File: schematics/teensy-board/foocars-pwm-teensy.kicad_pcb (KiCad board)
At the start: 2 copper layers, 26.4 x 36.6 mm, 4 parts, among them J1 TOPTOP-14-LEFT, J2 BOTTOMBOTTOM-14-LEFT, J3 PWM_Input, J4 PWM_Output

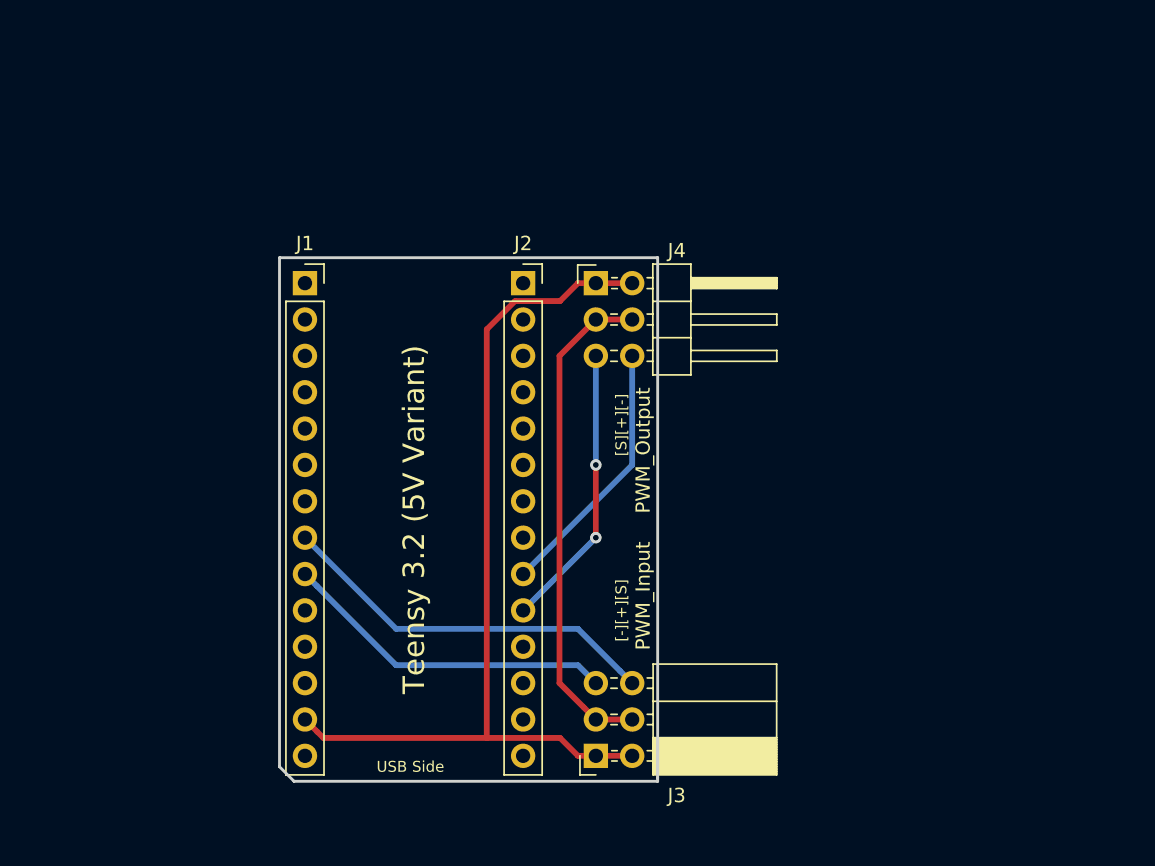
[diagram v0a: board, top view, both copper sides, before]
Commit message: Updated PWM hat to have new inputs.
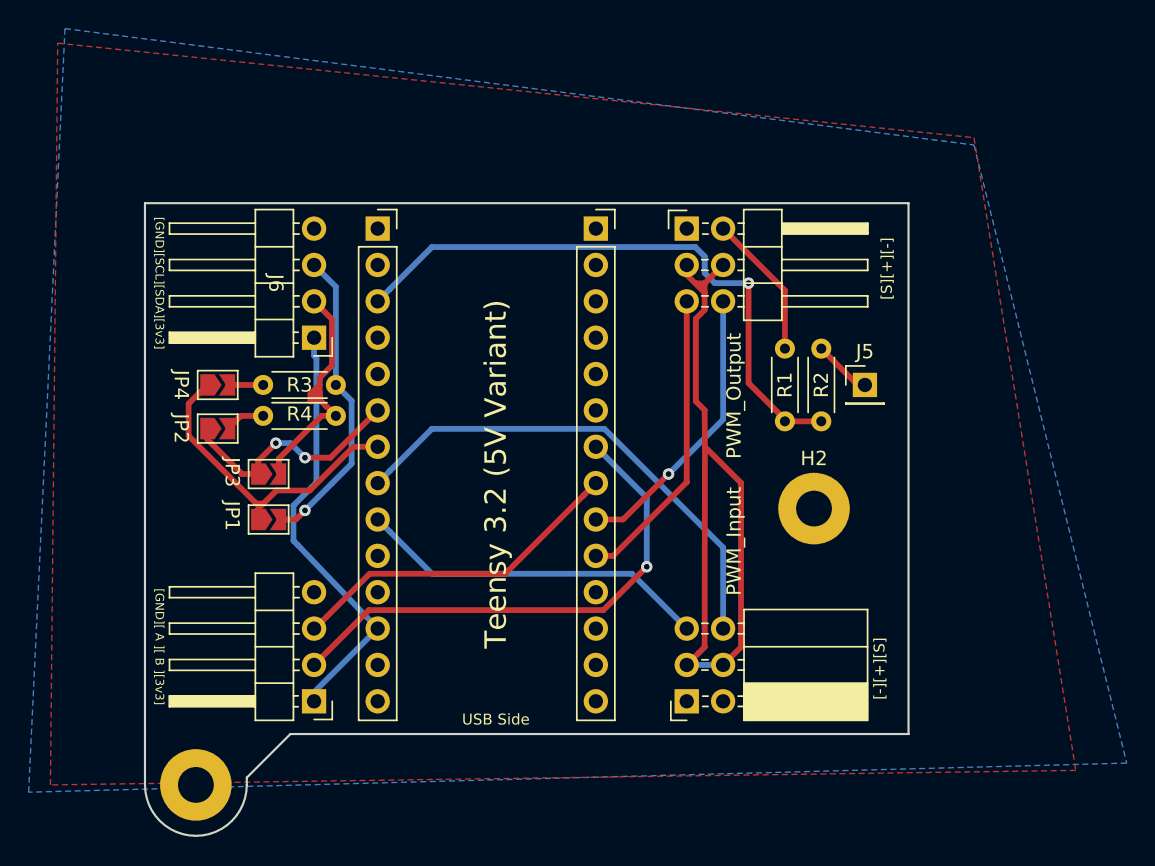
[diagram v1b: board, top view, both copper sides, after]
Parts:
- added H1: MountingHole, MountingHole:MountingHole_2.5mm_Pad, F.Cu at (152.4, 111.3)
- added H2: MountingHole, MountingHole:MountingHole_2.5mm_Pad, F.Cu at (195.6, 91.9)
- added J5: BattMon, Connector_PinHeader_2.54mm:PinHeader_1x01_P2.54mm_Vertical, F.Cu at (199.1, 83.3)
- added J6: Conn_01x04, Connector_PinHeader_2.54mm:PinHeader_1x04_P2.54mm_Horizontal, F.Cu at (160.7, 80.0)
- added J7: Conn_01x04, Connector_PinHeader_2.54mm:PinHeader_1x04_P2.54mm_Horizontal, F.Cu at (160.7, 105.4)
- added JP1: Jumper_2_Open, Jumper:SolderJumper-2_P1.3mm_Open_TrianglePad1.0x1.5mm, F.Cu at (157.5, 92.7)
- added JP2: Jumper_2_Open, Jumper:SolderJumper-2_P1.3mm_Open_TrianglePad1.0x1.5mm, F.Cu at (153.9, 83.3)
- added JP3: Jumper_2_Open, Jumper:SolderJumper-2_P1.3mm_Open_TrianglePad1.0x1.5mm, F.Cu at (157.5, 89.5)
- added JP4: Jumper_2_Open, Jumper:SolderJumper-2_P1.3mm_Open_TrianglePad1.0x1.5mm, F.Cu at (153.9, 86.4)
- added R1: R, Resistor_THT:R_Axial_DIN0204_L3.6mm_D1.6mm_P5.08mm_Horizontal, F.Cu at (193.5, 85.9)
- added R2: R, Resistor_THT:R_Axial_DIN0204_L3.6mm_D1.6mm_P5.08mm_Horizontal, F.Cu at (196.1, 80.8)
- added R3: R, Resistor_THT:R_Axial_DIN0204_L3.6mm_D1.6mm_P5.08mm_Horizontal, F.Cu at (157.1, 83.3)
- added R4: R, Resistor_THT:R_Axial_DIN0204_L3.6mm_D1.6mm_P5.08mm_Horizontal, F.Cu at (157.1, 85.5)
- J1: value TOPTOP-14-LEFT -> TOP_HALF
- J2: value BOTTOMBOTTOM-14-LEFT -> BOTTOM_HALF
- moved J3 7.41 mm to (186.7, 105.4)
- moved J4 7.41 mm to (186.7, 72.4)
- moved J2 6.35 mm to (180.3, 72.4)
- moved J1 6.35 mm to (165.1, 72.4)
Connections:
- J1 pad 1: (no net) -> Net-(J1-Pad1)
- J1 pad 10: (no net) -> Net-(J1-Pad10)
- J1 pad 11: (no net) -> Net-(J1-Pad11)
- J1 pad 12: (no net) -> 3v3
- J1 pad 13: GND -> Net-(J1-Pad13)
- J1 pad 14: (no net) -> Net-(J1-Pad14)
- J1 pad 2: (no net) -> Net-(J1-Pad2)
- J1 pad 3: (no net) -> Net-(J1-Pad3)
- J1 pad 4: (no net) -> Net-(J1-Pad4)
- J1 pad 5: (no net) -> Net-(J1-Pad5)
- J1 pad 6: (no net) -> SDA0
- J1 pad 7: (no net) -> SCL0
- J2 pad 1: (no net) -> Net-(J2-Pad1)
- J2 pad 11: (no net) -> Net-(J2-Pad11)
- J2 pad 12: (no net) -> Net-(J2-Pad12)
- J2 pad 13: (no net) -> Net-(J2-Pad13)
- J2 pad 14: (no net) -> GND
- J2 pad 2: (no net) -> Net-(J2-Pad2)
- J2 pad 3: (no net) -> Net-(J2-Pad3)
- J2 pad 4: (no net) -> Net-(J2-Pad4)
- J2 pad 5: (no net) -> Net-(J2-Pad5)
- J2 pad 6: (no net) -> Net-(J2-Pad6)
- J2 pad 7: (no net) -> Net-(J2-Pad7)
- J2 pad 8: (no net) -> Net-(J2-Pad8)
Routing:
- net GND: track 63.9 -> 10.2 mm
- net Net-(J1-Pad3): track 0.00 -> 42.4 mm, vias 0 -> 1
- net Net-(J2-Pad7): track 0.00 -> 35.9 mm, vias 0 -> 1
- net 3v3: track 0.00 -> 30.3 mm
- net Net-(J2-Pad8): track 0.00 -> 23.9 mm
- net SCL0: track 0.00 -> 22.2 mm
- net /SCL: track 0.00 -> 21.7 mm, vias 0 -> 1
- net /SDA: track 0.00 -> 19.5 mm
- net SDA0: track 0.00 -> 16.9 mm, vias 0 -> 2
- net Net-(J3-Pad3): track 35.1 -> 51.9 mm
- net Net-(J1-Pad8): track 27.1 -> 34.8 mm
- net Net-(J5-Pad1): track 0.00 -> 4.10 mm
- net Net-(JP4-Pad2): track 0.00 -> 2.82 mm
- net Net-(JP2-Pad2): track 0.00 -> 2.45 mm
- net Net-(J2-Pad9): track 18.4 -> 20.0 mm, vias 0 -> 1
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- added copper zone on B.Cu, net GND
- added copper zone on F.Cu, net GND
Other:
- board size 26.4 x 36.6 mm -> 53.3 x 44.2 mm
- board text added: "[GND][ A ][ B ][3v3]"
- board text added: "[GND][SCL][SDA][3v3]"

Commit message: Added new layout, new pins, added TVS diode.
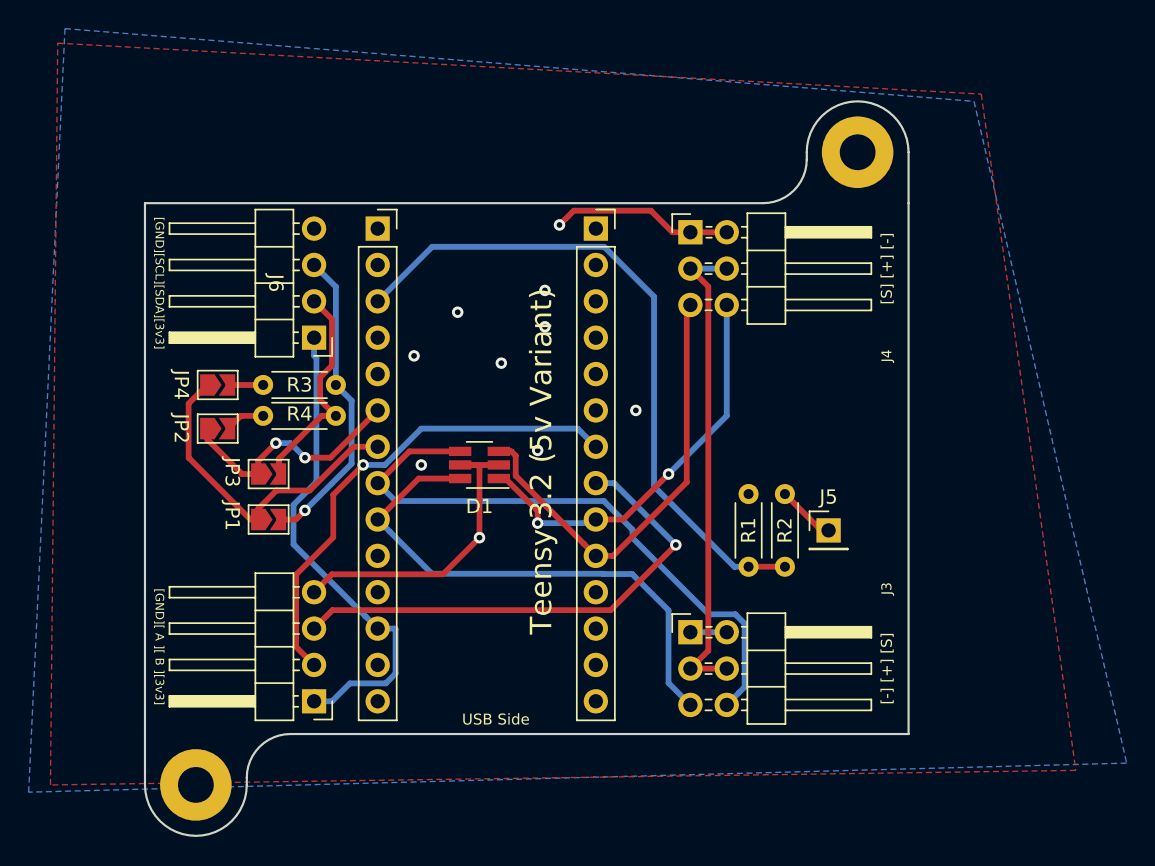
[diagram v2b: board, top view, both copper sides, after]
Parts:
- added D1: TVS Suppression, Package_TO_SOT_SMD:SOT-23-6_Handsoldering, F.Cu at (172.2, 88.9)
- J3: value PWM_Input -> Output; footprint Connector_PinSocket_2.54mm:PinSocket_2x03_P2.54mm_Horizontal -> Connector_PinHeader_2.54mm:PinHeader_2x03_P2.54mm_Horizontal
- J4: value PWM_Output -> Input
- moved H2 25.1 mm to (198.6, 67.1)
- moved J5 10.5 mm to (196.6, 93.5)
- moved R1 10.5 mm to (191.0, 96.0)
- moved R2 10.5 mm to (193.5, 90.9)
- moved J3 4.83 mm to (186.9, 100.6), turned to 0 degrees
- moved J4 0.36 mm to (186.9, 72.6)
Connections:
- net Net-(J3-Pad3) renamed VMOTORCONTROL
- J1 pad 1: Net-(J1-Pad1) -> (no net)
- J1 pad 10: Net-(J1-Pad10) -> (no net)
- J1 pad 11: Net-(J1-Pad11) -> (no net)
- J1 pad 13: Net-(J1-Pad13) -> (no net)
- J1 pad 14: Net-(J1-Pad14) -> (no net)
- J1 pad 2: Net-(J1-Pad2) -> (no net)
- J1 pad 4: Net-(J1-Pad4) -> (no net)
- J1 pad 5: Net-(J1-Pad5) -> (no net)
- J2 pad 1: Net-(J2-Pad1) -> (no net)
- J2 pad 11: Net-(J2-Pad11) -> (no net)
- J2 pad 12: Net-(J2-Pad12) -> (no net)
- J2 pad 13: Net-(J2-Pad13) -> (no net)
- J2 pad 2: Net-(J2-Pad2) -> (no net)
- J2 pad 3: Net-(J2-Pad3) -> (no net)
- J2 pad 4: Net-(J2-Pad4) -> (no net)
- J2 pad 5: Net-(J2-Pad5) -> (no net)
- J2 pad 6: Net-(J2-Pad6) -> (no net)
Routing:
- net GND: track 10.2 -> 37.4 mm, vias 0 -> 10
- net VMOTORCONTROL: track 51.9 -> 34.1 mm
- net Net-(D1-Pad6): track 24.7 -> 37.1 mm
- net Net-(J2-Pad8): track 23.9 -> 35.1 mm, vias 0 -> 1
- net Net-(D1-Pad3): track 21.1 -> 31.6 mm
- net Net-(D1-Pad1): track 20.0 -> 28.6 mm, vias 1 -> 2
- net Net-(D1-Pad4): track 34.8 -> 42.9 mm
- net Net-(J1-Pad3): track 42.4 -> 47.1 mm, vias 1 -> 0
- net 3v3: track 30.3 -> 35.0 mm
- net /SDA: track 19.5 -> 15.6 mm
- net Net-(J2-Pad7): track 35.9 -> 34.3 mm
- net SCL0: track 22.2 -> 23.2 mm
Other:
- board size 53.3 x 44.2 mm -> 53.3 x 51.3 mm
- board text added: "Teensy 3.2 (5v Variant)"
- board text added: "[-] [+] [S]"
- board text added: "[S] [+] [-]"
- board text removed: "Teensy 3.2 (5V Variant)"
- board text removed: "[-][+][S]"
- board text removed: "[S][+][-]"

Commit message: Swap ground pins, review with Rick.
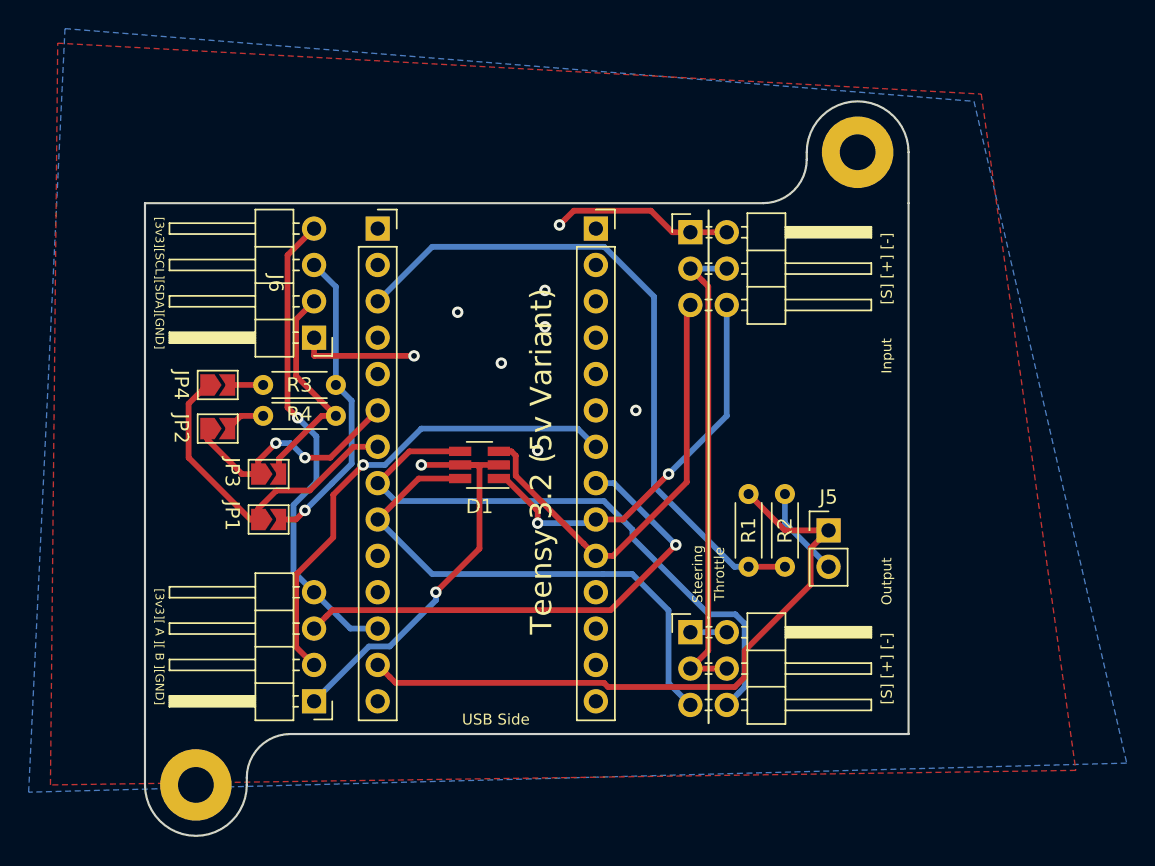
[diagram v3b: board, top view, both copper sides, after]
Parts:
- J5: footprint Connector_PinHeader_2.54mm:PinHeader_1x01_P2.54mm_Vertical -> Connector_PinHeader_2.54mm:PinHeader_1x02_P2.54mm_Vertical
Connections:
- J1 pad 13: (no net) -> Net-(J1-Pad13)
- J5 pad 1: Net-(J5-Pad1) -> Net-(J1-Pad13)
- J6 pad 1: 3v3 -> GND
- J6 pad 4: GND -> 3v3
- J7 pad 1: 3v3 -> GND
- J7 pad 4: GND -> 3v3
- R1 pad 2: GND -> Net-(J1-Pad13)
- R2 pad 1: Net-(J5-Pad1) -> Net-(J5-Pad2)
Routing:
- net Net-(J1-Pad13): track 0.00 -> 45.9 mm
- net GND: track 37.4 -> 52.6 mm
- net Net-(J5-Pad2): track 0.00 -> 6.34 mm
- net Net-(J5-Pad1): track 4.10 -> 0.00 mm
- net 3v3: track 35.0 -> 33.8 mm, vias 0 -> 1
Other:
- board text added: "Input"
- board text added: "Output"
- board text added: "Steering"
- board text added: "Throttle"
- board text added: "[3v3][ A ][ B ][GND]"
- board text added: "[3v3][SCL][SDA][GND]"
- board text removed: "[-] [+] [S]"
- board text removed: "[GND][ A ][ B ][3v3]"
- board text removed: "[GND][SCL][SDA][3v3]"
